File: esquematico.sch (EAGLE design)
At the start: 60 parts, among them IC1 AM29F010P, IC10 74AC11034, IC11 74AC11238, IC13 74AC11008, IC14 74AC11034, IC15 74AC11008, IC16 74AC11034, IC17 74AC11008, IC18 74AC11034, IC19 74AC11008, IC2 74AC373N, IC20 74AC11034, IC21 74AC11008, IC22 74AC11034, IC23 74AC11008, IC24 74AC11034, IC25 74AC11008, IC26 74AC11034, IC27 74AC11008, IC3 AT89S52, IC31 4572D, IC32 74159N, IC33 4572D, IC34 4572D, IC35 4572D, IC36 4572D, IC4 AM29F010P, IC5 4075N, IC6 74AC06N, IC7 4503D, IC8 74AC373N, IC9 MAX233, Q1 11.0592 MHz

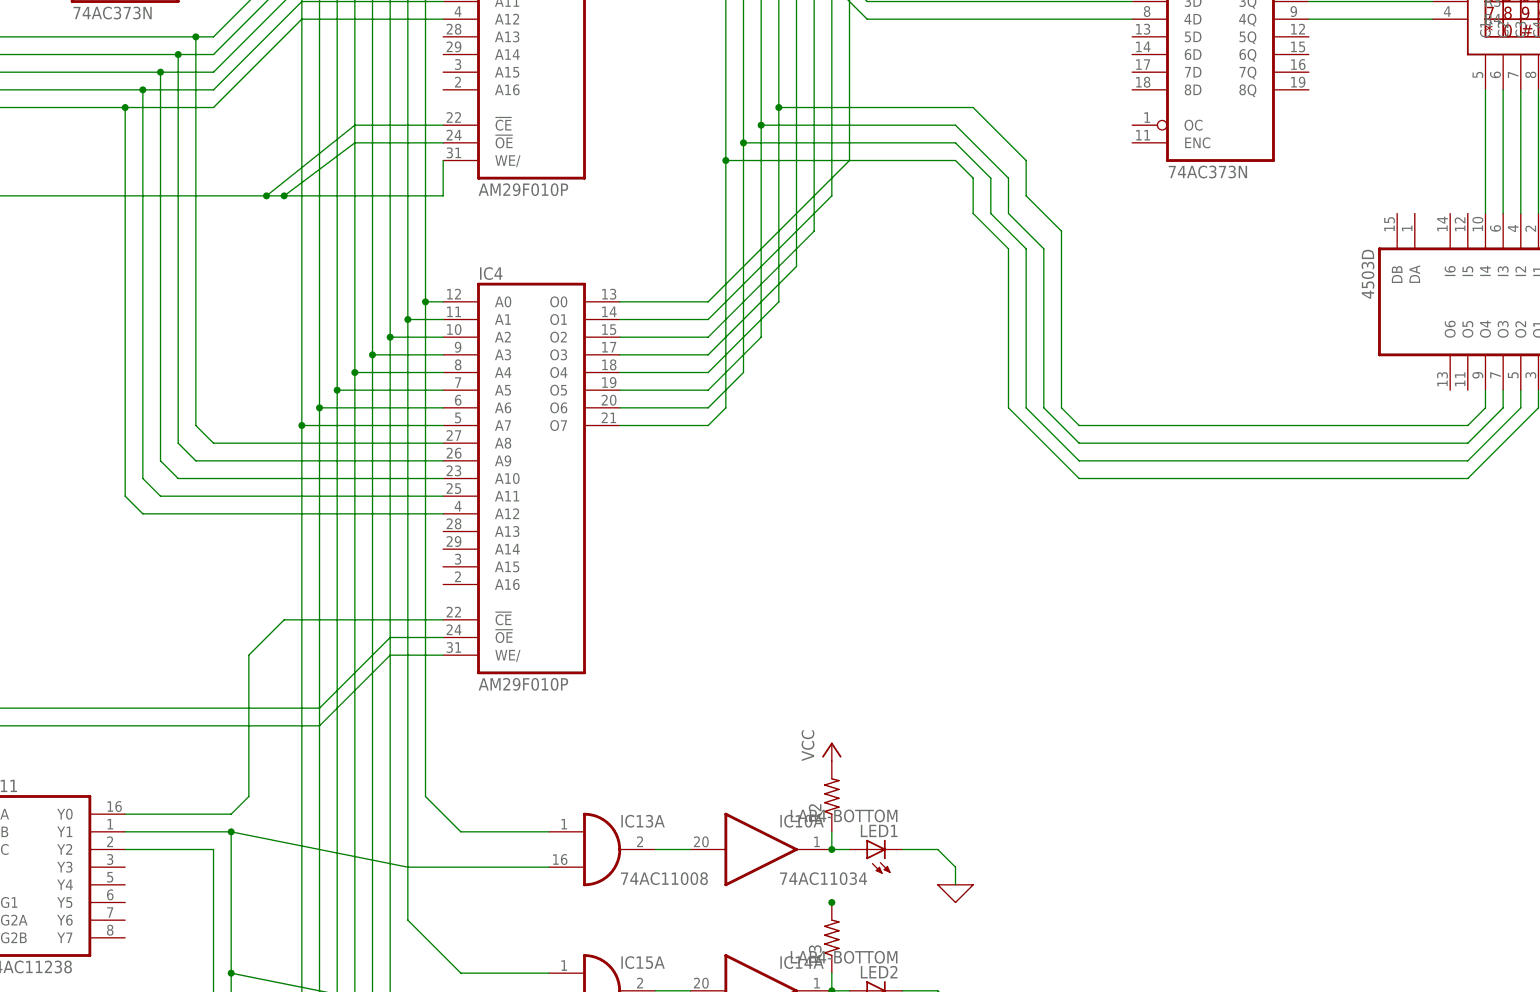
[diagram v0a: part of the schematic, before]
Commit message: Code for keypad reading and motors
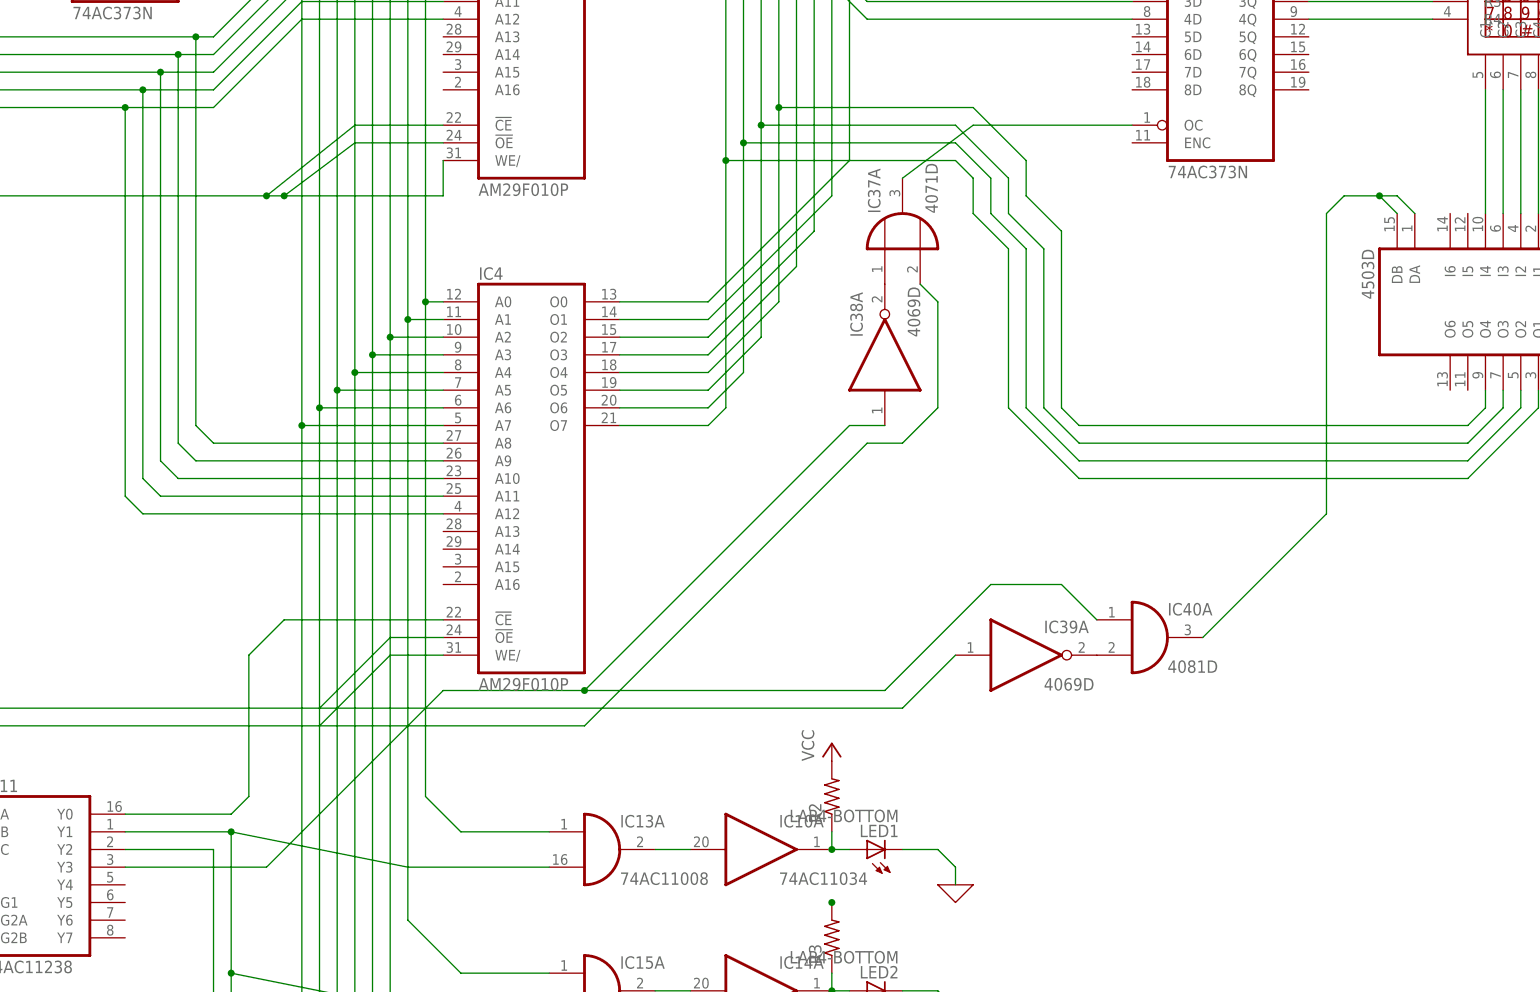
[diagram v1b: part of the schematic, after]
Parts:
- added IC37: 4071D, 40xx:4071D
- added IC38, IC39: 4069D, 40xx:4069D
- added IC40: 4081D, 40xx:4081D
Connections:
- new net N$84: IC11A.Y3, IC38A.I, IC40A.I0
- new net N$86: IC37A.O, IC8A.OC
- new net N$88: IC37A.I0, IC38A.O
- new net N$89: IC39A.O, IC40A.I1
- new net N$90: IC40A.O, IC7A.DA, IC7A.DB
- net N$29: now also IC37A.I1
- net N$32: now also IC39A.I
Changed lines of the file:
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@@
 <setting verticaltext="up"/>
 </settings>
-<grid distance="0.1" unitdist="inch" unit="inch" style="lines" multiple="1" display="yes" altdistance="0.01" altunitdist="inch" altunit="inch"/>
+<grid distance="0.1" unitdist="inch" unit="inch" style="lines" multiple="1" display="no" altdistance="0.01" altunitdist="inch" altunit="inch"/>
 <layers>
 <layer number="1" name="Top" color="4" fill="1" visible="no" active="no"/>
@@
 <part name="IC35" library="45xx" library_urn="urn:adsk.eagle:library:82" deviceset="4572" device="D" package3d_urn="urn:adsk.eagle:package:1005/2"/>
 <part name="IC36" library="45xx" library_urn="urn:adsk.eagle:library:82" deviceset="4572" device="D" package3d_urn="urn:adsk.eagle:package:1005/2"/>
+<part name="IC37" library="40xx" library_urn="urn:adsk.eagle:library:80" deviceset="4071" device="D" package3d_urn="urn:adsk.eagle:package:823/2"/>
+<part name="IC38" library="40xx" library_urn="urn:adsk.eagle:library:80" deviceset="4069" device="D" package3d_urn="urn:adsk.eagle:package:823/2"/>
+<part name="IC39" library="40xx" library_urn="urn:adsk.eagle:library:80" deviceset="4069" device="D" package3d_urn="urn:adsk.eagle:package:823/2"/>
+<part name="IC40" library="40xx" library_urn="urn:adsk.eagle:library:80" deviceset="4081" device="D" package3d_urn="urn:adsk.eagle:package:823/2"/>
 </parts>
 <sheets>
@@
 <instance part="IC35" gate="A" x="45.72" y="-228.6"/>
 <instance part="IC36" gate="A" x="121.92" y="-236.22"/>
+<instance part="IC37" gate="A" x="276.86" y="7.62" rot="R90"/>
+<instance part="IC38" gate="A" x="274.32" y="-10.16" rot="R90"/>
+<instance part="IC39" gate="A" x="294.64" y="-53.34"/>
+<instance part="IC40" gate="A" x="312.42" y="-50.8"/>
 </instances>
 <busses>
@@
 <pinref part="IC4" gate="G$1" pin="WE/"/>
 <wire x1="203.2" y1="-53.34" x2="210.82" y2="-53.34" width="0.1524" layer="91"/>
+<wire x1="193.04" y1="-63.5" x2="231.14" y2="-63.5" width="0.1524" layer="91"/>
+<wire x1="231.14" y1="-63.5" x2="271.78" y2="-22.86" width="0.1524" layer="91"/>
+<wire x1="271.78" y1="-22.86" x2="276.86" y2="-22.86" width="0.1524" layer="91"/>
+<wire x1="276.86" y1="-22.86" x2="281.94" y2="-17.78" width="0.1524" layer="91"/>
+<pinref part="IC37" gate="A" pin="I1"/>
+<wire x1="281.94" y1="-17.78" x2="281.94" y2="-2.54" width="0.1524" layer="91"/>
+<wire x1="281.94" y1="-2.54" x2="279.4" y2="0" width="0.1524" layer="91"/>
 </segment>
 </net>
@@
 <pinref part="IC3" gate="P" pin="P3.7/!RD"/>
 <wire x1="63.5" y1="12.7" x2="66.04" y2="15.24" width="0.1524" layer="91"/>
+<pinref part="IC39" gate="A" pin="I"/>
+<wire x1="193.04" y1="-60.96" x2="276.86" y2="-60.96" width="0.1524" layer="91"/>
+<wire x1="276.86" y1="-60.96" x2="284.48" y2="-53.34" width="0.1524" layer="91"/>
 </segment>
 </net>
@@
 </segment>
 </net>
+<net name="N$84" class="0">
+<segment>
+<pinref part="IC11" gate="A" pin="Y3"/>
+<wire x1="165.1" y1="-83.82" x2="185.42" y2="-83.82" width="0.1524" layer="91"/>
+<wire x1="185.42" y1="-83.82" x2="210.82" y2="-58.42" width="0.1524" layer="91"/>
+<wire x1="210.82" y1="-58.42" x2="231.14" y2="-58.42" width="0.1524" layer="91"/>
+<pinref part="IC38" gate="A" pin="I"/>
+<wire x1="231.14" y1="-58.42" x2="269.24" y2="-20.32" width="0.1524" layer="91"/>
+<wire x1="269.24" y1="-20.32" x2="274.32" y2="-20.32" width="0.1524" layer="91"/>
+<wire x1="231.14" y1="-58.42" x2="274.32" y2="-58.42" width="0.1524" layer="91"/>
+<wire x1="274.32" y1="-58.42" x2="289.56" y2="-43.18" width="0.1524" layer="91"/>
+<junction x="231.14" y="-58.42"/>
+<pinref part="IC40" gate="A" pin="I0"/>
+<wire x1="289.56" y1="-43.18" x2="299.72" y2="-43.18" width="0.1524" layer="91"/>
+<wire x1="299.72" y1="-43.18" x2="304.8" y2="-48.26" width="0.1524" layer="91"/>
+</segment>
+</net>
+<net name="N$86" class="0">
+<segment>
+<pinref part="IC37" gate="A" pin="O"/>
+<pinref part="IC8" gate="A" pin="OC"/>
+<wire x1="276.86" y1="15.24" x2="287.02" y2="22.86" width="0.1524" layer="91"/>
+<wire x1="287.02" y1="22.86" x2="309.88" y2="22.86" width="0.1524" layer="91"/>
+</segment>
+</net>
+<net name="N$88" class="0">
+<segment>
+<pinref part="IC37" gate="A" pin="I0"/>
+<pinref part="IC38" gate="A" pin="O"/>
+</segment>
+</net>
+<net name="N$89" class="0">
+<segment>
+<pinref part="IC39" gate="A" pin="O"/>
+<pinref part="IC40" gate="A" pin="I1"/>
+</segment>
+</net>
+<net name="N$90" class="0">
+<segment>
+<pinref part="IC40" gate="A" pin="O"/>
+<wire x1="320.04" y1="-50.8" x2="337.82" y2="-33.02" width="0.1524" layer="91"/>
+<wire x1="337.82" y1="-33.02" x2="337.82" y2="10.16" width="0.1524" layer="91"/>
+<wire x1="337.82" y1="10.16" x2="340.36" y2="12.7" width="0.1524" layer="91"/>
+<wire x1="340.36" y1="12.7" x2="345.44" y2="12.7" width="0.1524" layer="91"/>
+<pinref part="IC7" gate="A" pin="DB"/>
+<wire x1="345.44" y1="12.7" x2="347.98" y2="10.16" width="0.1524" layer="91"/>
+<pinref part="IC7" gate="A" pin="DA"/>
+<wire x1="345.44" y1="12.7" x2="347.98" y2="12.7" width="0.1524" layer="91"/>
+<wire x1="347.98" y1="12.7" x2="350.52" y2="10.16" width="0.1524" layer="91"/>
+<junction x="345.44" y="12.7"/>
+</segment>
+</net>

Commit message: Add files via upload
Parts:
- added DIS1: TUXGR_16X2_R2, display-lcd:TUXGR_16X2_R2
- added IC41, IC42: 4572D, 45xx:4572D
- added IC43, IC44: 74ALS873NT, 74xx-eu:74ALS873NT
- added IC45: 74AC373DW, 74xx-eu:74AC373DW
- added IC46: MAX161ACP, maxim:MAX161ACP
- added IC47: 74AC573D, 74xx-eu:74AC573D
- added IC48, IC50, IC53: 4081D, 40xx:4081D
- added IC49, IC52: 4069D, 40xx:4069D
- added IC51: MC1408D, linear:MC1408D
- added IC54: 74ALS845NT, 74xx-eu:74ALS845NT
- added IC55: AD822N, analog-devices:AD822N
- added R10: 5.000k, rcl:R-US_0204/2V
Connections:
- removed net N$15: IC17A.I0, IC1G$1.A2, IC2A.3Q, IC4G$1.A2
- removed net N$19: IC1G$1.A6, IC25A.I0, IC2A.7Q, IC4G$1.A6
- new net N$100: DIS1.D5, IC45A.6Q
- new net N$101: DIS1.D6, IC45A.7Q
- new net N$102: DIS1.D7, IC45A.8Q
- new net N$103: IC42A.O, IC44A.CLR, IC44A.OC
- new net N$104: IC43A.Q1, IC46.A0
- new net N$105: IC41A.O, IC45A.OC
- new net N$106: IC43A.Q2, IC46.A1
- new net N$107: IC43A.Q3, IC46.A2
- new net N$108: IC43A.Q4, IC46.CS
- new net N$109: IC46.DB7, IC47A.8D
- new net N$110: IC46.DB6, IC47A.7D
- new net N$111: IC46.DB5, IC47A.6D
- new net N$112: IC46.DB4, IC47A.5D
- new net N$113: IC46.DB3, IC47A.4D
- new net N$114: IC46.DB1, IC47A.2D
- new net N$115: IC46.DB2, IC47A.3D
- new net N$116: IC46.DB0, IC47A.1D
- new net N$117: IC41A.I, IC48B.O
- new net N$118: IC49B.I, IC50C.O
- new net N$121: IC43A.OC, IC49B.O
- new net N$122: IC11A.Y5, IC40C.I0, IC50C.I0, IC53C.I0
- new net N$123: IC38B.I, IC40C.O
- new net N$124: IC38B.O, IC47A.OC
- new net N$125: IC52B.I, IC53C.O
- new net N$127: IC52B.O, IC54A.OC1, IC54A.OC2, IC54A.OC3
- new net N$129: IC1G$1.A6, IC25A.I0, IC2A.7Q, IC45A.7D, IC47A.7Q, IC4G$1.A6, IC54A.7D
- new net N$131: IC17A.I0, IC1G$1.A2, IC2A.3Q, IC43A.D3, IC44A.D3, IC45A.3D, IC47A.3Q, IC4G$1.A2, IC54A.3D
- new net N$134: IC51.A1, IC54A.1Q
- new net N$135: IC51.A2, IC54A.2Q
- new net N$136: IC51.A3, IC54A.3Q
- new net N$137: IC51.A4, IC54A.4Q
- new net N$138: IC51.A5, IC54A.5Q
- new net N$139: IC51.A6, IC54A.6Q
- new net N$140: IC51.A7, IC54A.7Q
- new net N$141: IC51.A8, IC54A.8Q
- new net N$142: IC51.IO, IC55A.IN-, R10.1
- new net N$144: IC55A.OUT, R10.2
- new net N$91: IC11A.Y4, IC40B.I1, IC48B.I1
- new net N$92: DIS1.E, IC44A.Q3
- new net N$93: DIS1.R/W, IC44A.Q2
- new net N$94: DIS1.RS, IC44A.Q1
- new net N$95: DIS1.D0, IC45A.1Q
- new net N$96: DIS1.D1, IC45A.2Q
- new net N$97: DIS1.D2, IC45A.3Q
- new net N$98: DIS1.D3, IC45A.4Q
- new net N$99: DIS1.D4, IC45A.5Q
- net 0: now also IC55A.IN+
- net N$13: now also IC43A.D1, IC44A.D1, IC45A.1D, IC47A.1Q, IC54A.1D
- net N$14: now also IC43A.D2, IC44A.D2, IC45A.2D, IC47A.2Q, IC54A.2D
- net N$16: now also IC43A.D4, IC45A.4D, IC47A.4Q, IC54A.4D
- net N$17: now also IC45A.5D, IC47A.5Q, IC54A.5D
- net N$18: now also IC45A.8D, IC47A.8Q, IC54A.8D
- net N$21: now also IC40B.I0, IC40C.I1
- net N$22: now also IC48B.I0, IC50C.I1
- net N$23: now also IC53C.I1
- net N$33: now also IC45A.6D, IC47A.6Q, IC54A.6D
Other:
- moved on the sheet: IC10A, IC11, IC13A, IC14A, IC15A, IC16A, IC17A, IC18A, IC19A, IC20A, IC21A, IC22A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

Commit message: Add files via upload
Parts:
- added IC56, IC57, IC58, IC59, IC60: 4081D, 40xx:4081D
- added OK1: AEDR-8300-K/P/Q, optocoupler:AEDR-8300-K/P/Q
- added XR1: HFD3000, opto-honeywell:HFD3000
- IC11: value 74AC11238 -> 74ALS873NT; device 74ac-logic:74AC11238 -> 74xx-eu:74ALS873NT
- IC42: value 4572D -> 4081D; device 45xx:4572D -> 40xx:4081D
- IC5: value 4075N -> 74AC11238; device 40xx:4075N -> 74ac-logic:74AC11238
- IC6: value 74AC06N -> 74ALS873NT; device 74xx-eu:74AC06N -> 74xx-eu:74ALS873NT
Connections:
- removed net N$52 (its old number): IC5A.I2
- new net N$119: IC3.P3.4/T0, OK1G$1.CHA
- new net N$120: IC58A.O, IC59A.I0
- new net N$126: IC59A.I1, IC60A.O
- new net N$128: IC3.P3.3/!INT1, IC59A.O
- new net N$15: IC38C.I, XR1.OUT
- new net N$19: IC3.P3.2/!INT0, IC38C.O
- new net N$94: IC11A.C, IC56B.O
- net N$10: now also IC47A.1Q, IC54A.1D
- net N$103: now also IC57B.O, IC6A.C; no longer IC42A.O, IC44A.CLR, IC44A.OC
- net N$108: now also IC46.CLK; no longer IC46.CS
- net N$11: now also IC47A.8Q, IC54A.8D, IC60A.I1
- net N$122: now also IC5A.Y6; no longer IC11A.Y5
- net N$129: no longer IC47A.7Q, IC54A.7D
- net N$13: no longer IC47A.1Q, IC54A.1D
- net N$131: now also IC6A.D3; no longer IC44A.D3, IC47A.3Q, IC54A.3D
- net N$14: now also IC11A.D2; no longer IC44A.D2, IC47A.2Q, IC54A.2D
- net N$16: now also IC42B.I0; no longer IC47A.4Q, IC54A.4D
- net N$17: now also IC56B.I0; no longer IC47A.5Q, IC54A.5D
- net N$18: no longer IC47A.8Q, IC54A.8D
- net N$20: now also IC5A.C; no longer IC11A.C
- net N$25: now also IC5A.B; no longer IC11A.B
- net N$26: now also DIS1.R/W, IC11A.Q2; no longer IC5A.I1
- net N$33: now also IC57B.I0; no longer IC47A.6Q, IC54A.6D
- net N$36: now also IC47A.7Q, IC54A.7D, IC60A.I0
- net N$37: now also IC47A.4Q, IC54A.4D
- net N$39: now also IC47A.2Q, IC54A.2D
- net N$4: now also DIS1.E, IC6A.Q3; no longer IC5A.I0, IC6A.O
- net N$42: now also IC47A.5Q, IC54A.5D, IC58A.I0
- net N$5: now also IC5A.Y1; no longer IC11A.Y0
- net N$51: now also IC5A.A; no longer IC11A.A
- net N$6: now also IC47A.3Q, IC54A.3D
- net N$63: now also IC5A.Y3; no longer IC11A.Y2
- net N$69: now also IC5A.Y2; no longer IC11A.Y1
- net N$7: now also IC47A.6Q, IC54A.6D, IC58A.I1
- net N$84: now also IC5A.Y4; no longer IC11A.Y3
- net N$91: now also IC5A.Y5; no longer IC11A.Y4
- net N$92: now also IC40B.O, IC42B.I1, IC56B.I1, IC57B.I1; no longer DIS1.E, IC44A.Q3
- net N$93: now also IC42B.O, IC44A.C; no longer DIS1.R/W, IC44A.Q2
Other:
- moved on the sheet: DIS1, IC40B, IC44A, IC45

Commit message: Add files via upload
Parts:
- removed IC1: AM29F010P, am29-memory:AM29F010P
- added IC61: 74AC16373, 74ac-logic:74AC16373
- IC32: value 74159N -> 27C080J; device 74xx-eu:74159N -> atmel:27C080J
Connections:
- net N$10: now also IC32G$1.O0; no longer IC1G$1.O0
- net N$11: now also IC32G$1.O7; no longer IC1G$1.O7
- net N$129: now also IC32G$1.A6, IC61G$1.1D7; no longer IC1G$1.A6
- net N$13: now also IC32G$1.A0, IC61G$1.1D1; no longer IC1G$1.A0
- net N$131: now also IC32G$1.A2, IC61G$1.1D3; no longer IC1G$1.A2
- net N$14: now also IC32G$1.A1, IC61G$1.1D2; no longer IC1G$1.A1
- net N$16: now also IC32G$1.A3, IC61G$1.1D4; no longer IC1G$1.A3
- net N$17: now also IC32G$1.A4, IC61G$1.1D5; no longer IC1G$1.A4
- net N$18: now also IC32G$1.A7, IC61G$1.1D8; no longer IC1G$1.A7
- net N$21: now also IC32G$1.A8; no longer IC1G$1.A8
- net N$22: now also IC32G$1.A9; no longer IC1G$1.A9
- net N$23: now also IC32G$1.A10; no longer IC1G$1.A10
- net N$24: now also IC32G$1.A11; no longer IC1G$1.A11
- net N$28: now also IC32G$1.A12; no longer IC1G$1.A12
- net N$31: no longer IC1G$1.!CE, IC1G$1.!OE, IC1G$1.WE/
- net N$33: now also IC32G$1.A5, IC61G$1.1D6; no longer IC1G$1.A5
- net N$36: now also IC32G$1.O6; no longer IC1G$1.O6
- net N$37: now also IC32G$1.O3; no longer IC1G$1.O3
- net N$39: now also IC32G$1.O1; no longer IC1G$1.O1
- net N$42: now also IC32G$1.O4; no longer IC1G$1.O4
- net N$53: now also IC61G$1.1OE, IC61G$1.2OE; no longer IC32A.G1, IC32A.G2
- net N$54: now also IC61G$1.1Q1; no longer IC32A.0
- net N$57: now also IC61G$1.1Q2; no longer IC32A.1
- net N$6: now also IC32G$1.O2; no longer IC1G$1.O2
- net N$60: now also IC61G$1.1Q3; no longer IC32A.2
- net N$7: now also IC32G$1.O5; no longer IC1G$1.O5
- net N$72: now also IC61G$1.1Q4; no longer IC32A.3
- net N$75: now also IC61G$1.1Q5; no longer IC32A.4
- net N$76: now also IC61G$1.1Q6; no longer IC32A.5
- net N$77: now also IC61G$1.1Q7; no longer IC32A.6
- net N$78: now also IC61G$1.1Q8; no longer IC32A.7
- net N$79: now also IC61G$1.2Q1; no longer IC32A.8
- net N$80: now also IC61G$1.2Q2; no longer IC32A.9
- net N$81: now also IC61G$1.2Q3; no longer IC32A.10
- net N$83: now also IC61G$1.2Q4; no longer IC32A.11
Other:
- moved on the sheet: IC31A
